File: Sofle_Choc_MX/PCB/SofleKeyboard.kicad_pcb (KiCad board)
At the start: 2 copper layers, 143.4 x 111.8 mm, 84 parts, among them J2 4PIN, J3 OLED, P1 i2c_pin, P2 i2c_pin, SW1 SW_PUSH_LED, SW10 SW_PUSH_LED, SW11 SW_PUSH_LED, SW12 SW_PUSH_LED, SW13 SW_PUSH_LED, SW14 SW_PUSH_LED, SW15 SW_PUSH_LED, SW16 SW_PUSH_LED, SW17 SW_PUSH_LED, SW18 SW_PUSH_LED, SW19 SW_PUSH_LED, SW2 SW_PUSH_LED, SW20 SW_PUSH_LED, SW21 SW_PUSH_LED, SW22 SW_PUSH_LED, SW23 SW_PUSH_LED, SW24 SW_PUSH_LED, SW25 Rotary_Encoder_Switch, SW26 SW_PUSH_LED, SW27 SW_PUSH_LED, SW28 SW_PUSH_LED, SW29 SW_PUSH_LED, SW3 SW_PUSH_LED, SW30 SW_PUSH_LED, SW4 SW_PUSH_LED, SW5 SW_PUSH_LED, SW6 SW_PUSH_LED, SW7 SW_PUSH_LED, SW8 SW_PUSH_LED, SW9 SW_PUSH_LED, U1 ProMicro

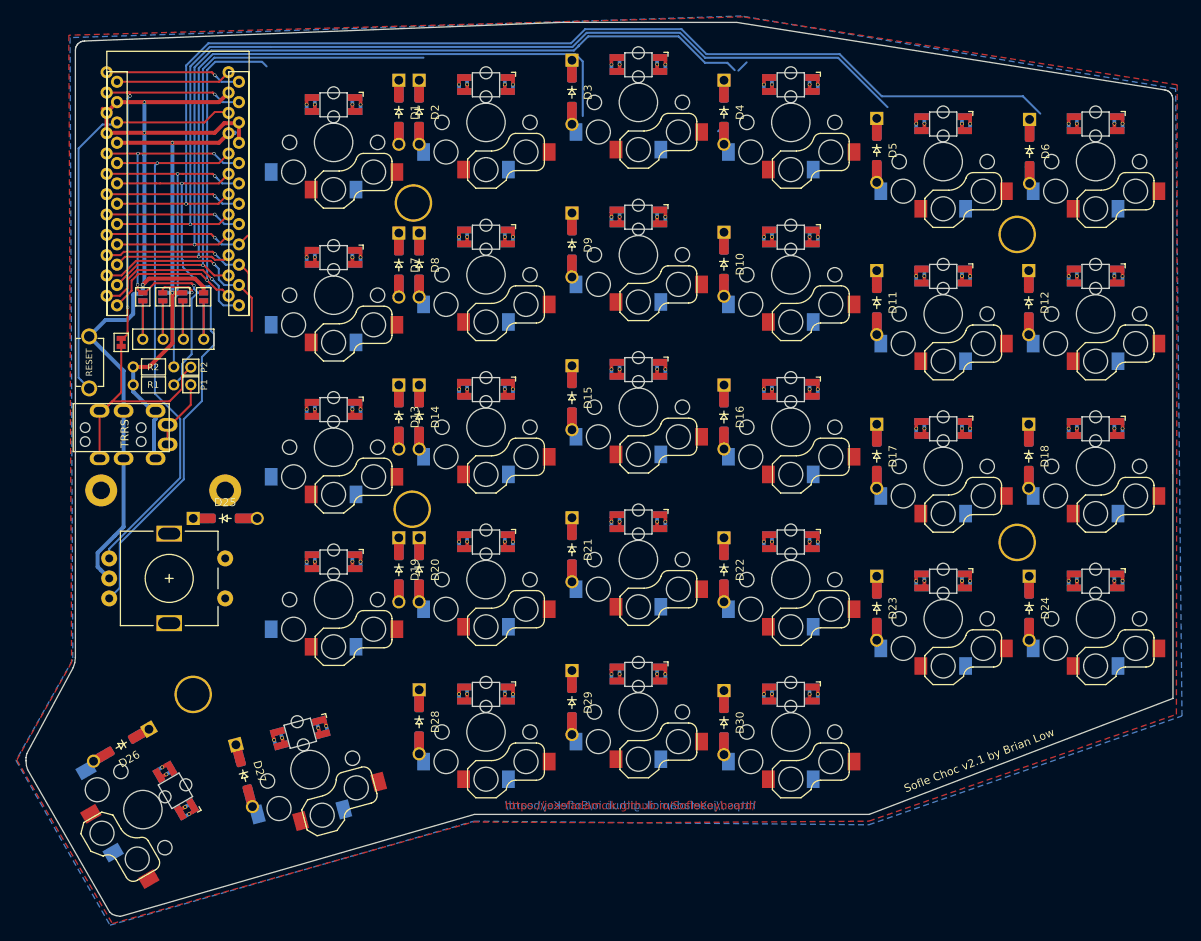
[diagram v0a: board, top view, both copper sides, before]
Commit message: Diodes moved to prevent footprint overlaps
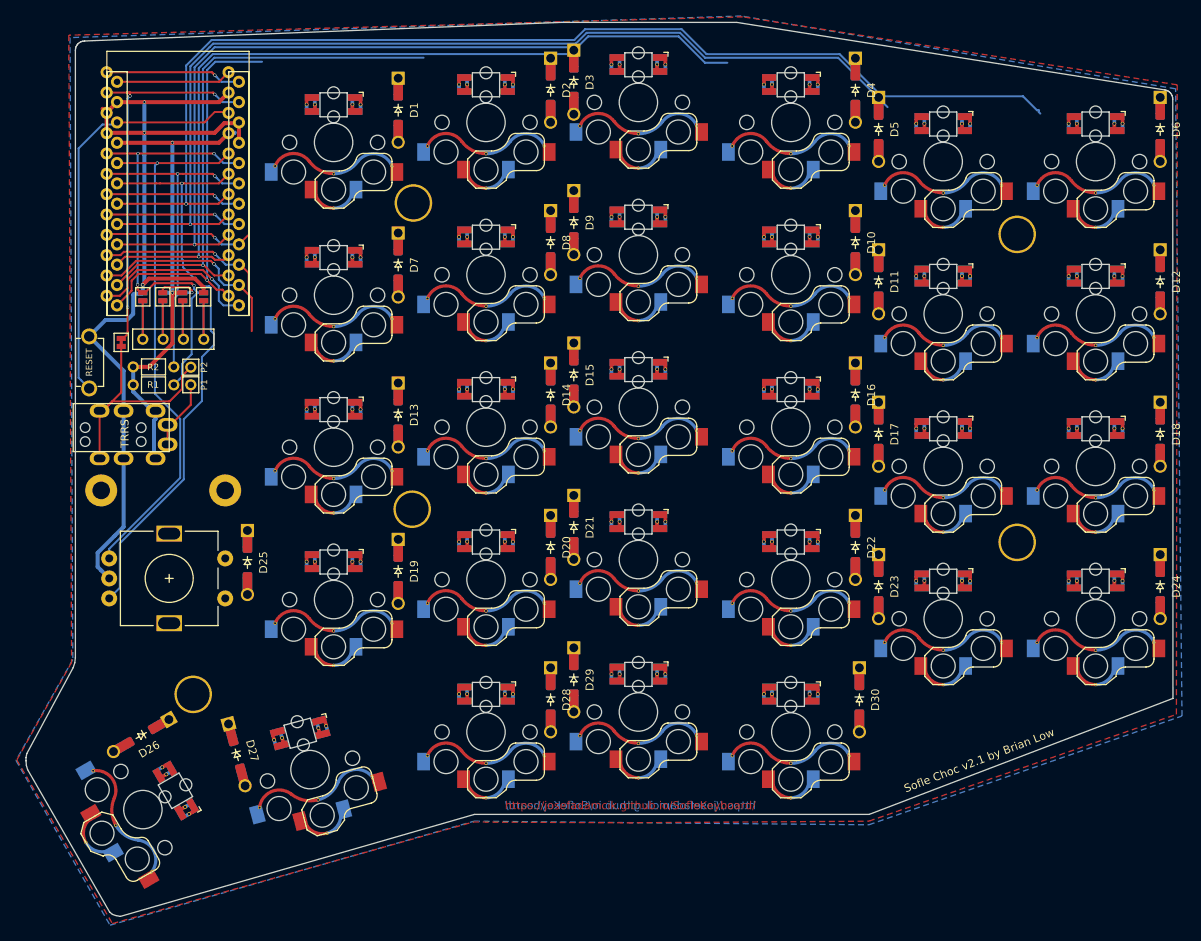
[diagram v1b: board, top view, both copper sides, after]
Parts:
- moved D30 17.2 mm to (186.3, 119.7)
- moved D20 16.7 mm to (147.7, 100.6)
- moved D22 16.7 mm to (185.8, 100.6)
- moved D8 16.7 mm to (147.7, 62.5)
- moved D14 16.7 mm to (147.7, 81.6)
- moved D16 16.7 mm to (185.8, 81.6)
- moved D18 16.7 mm to (223.9, 86.5)
- moved D2 16.7 mm to (147.7, 43.5)
- moved D28 16.7 mm to (147.7, 119.7)
- moved D4 16.7 mm to (185.8, 43.5)
- moved D10 16.7 mm to (185.8, 62.5)
- moved D12 16.6 mm to (223.9, 67.4)
- moved D24 16.6 mm to (223.9, 105.5)
- moved D6 16.6 mm to (223.9, 48.4)
- moved D25 6.17 mm to (109.8, 102.5), turned to -90 degrees
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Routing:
- net col3: track 95.2 -> 87.1 mm
- net Net-(SW4-Pad2): track 1.47 -> 0.00 mm
- net col2: track 107.8 -> 106.5 mm
- net row0: track 18.3 -> 17.1 mm
- net Net-(D4-Pad2): track 1.05 -> 0.00 mm
- net SW25A: track 51.9 -> 51.1 mm

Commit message: Switch footprint overhaul switch rerouteing
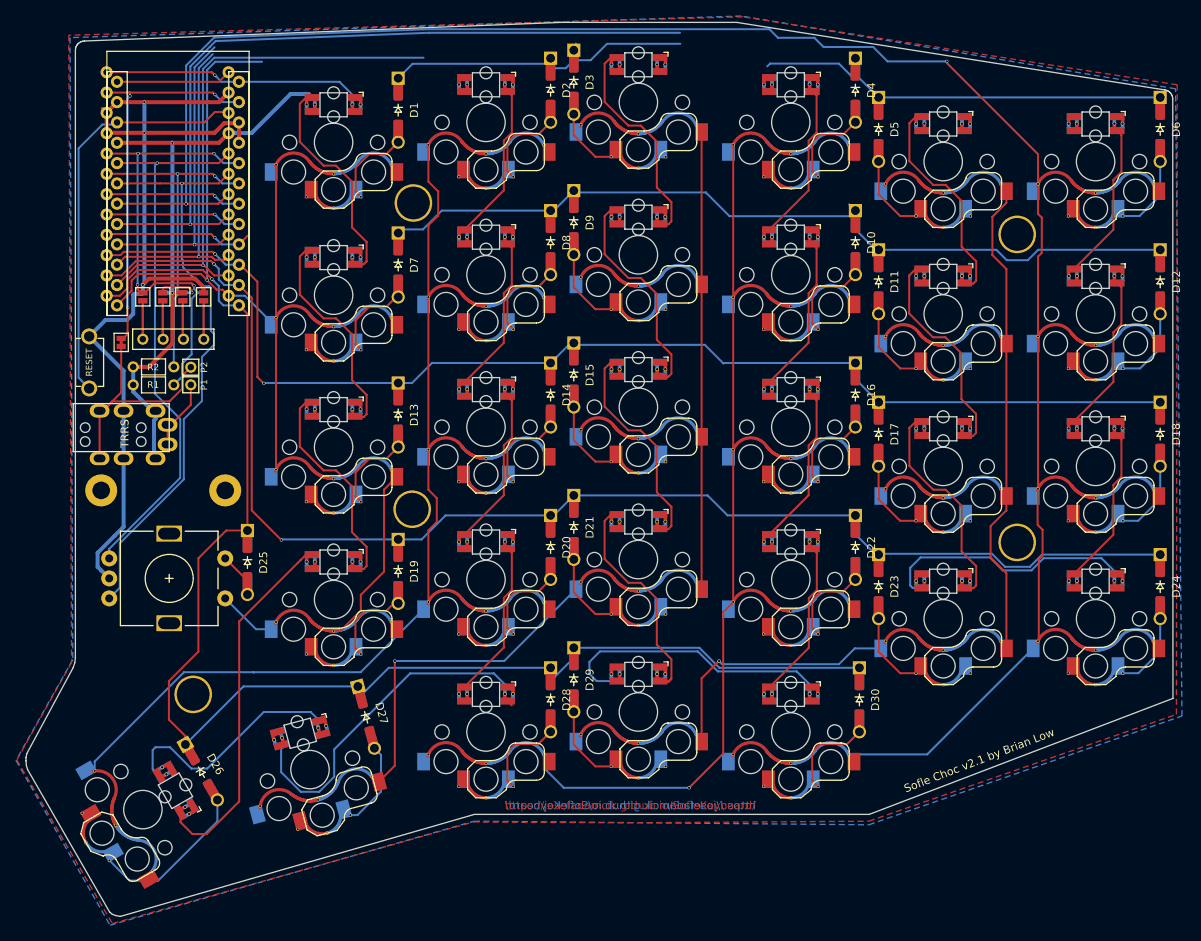
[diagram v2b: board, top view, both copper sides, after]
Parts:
- moved D27 16.8 mm to (124.6, 121.9)
- moved D26 8.81 mm to (104.0, 128.7), turned to -60 degrees
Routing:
- net row4: track 21.6 -> 173.9 mm
- net row3: track 25.8 -> 169.0 mm, vias 1 -> 2
- net row2: track 21.1 -> 150.8 mm, vias 1 -> 2
- net col4: track 68.7 -> 178.0 mm
- net row1: track 18.6 -> 120.9 mm
- net col0: track 145.1 -> 236.9 mm, vias 1 -> 2
- net row0: track 17.1 -> 106.0 mm
- net SW25A: track 51.1 -> 126.6 mm
- net col1: track 126.9 -> 189.3 mm, vias 1 -> 2
- net col3: track 87.1 -> 143.0 mm, vias 1 -> 2
- net Net-(SW19-Pad2): track 0.00 -> 46.4 mm
- net Net-(SW27-Pad2): track 0.00 -> 42.3 mm
- net col2: track 106.5 -> 143.8 mm, vias 1 -> 2
- net Net-(SW29-Pad2): track 0.00 -> 35.5 mm
- net Net-(SW23-Pad2): track 0.00 -> 32.3 mm
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- added copper zone on F.Cu, net GND
- added copper zone on B.Cu, net VCC
- removed copper zone on B.Cu, net GND
- removed copper zone on F.Cu, net VCC
